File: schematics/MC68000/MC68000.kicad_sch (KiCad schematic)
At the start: 0 parts

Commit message: first commit
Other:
- note added: "CPU MC68000 CLOCK 16MHZ DATA AND ADDRESS BUFFERS HALT AND RESET DTACK GLUE LOGIC"
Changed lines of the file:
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@@
 (kicad_sch (version 20230121) (generator eeschema)
   (paper "A3")
-  (sheet (at 31.75 31.75) (size 60.96 16.51) (fields_autoplaced)
+  (text "CPU MC68000 \nCLOCK 16MHZ\nDATA AND ADDRESS BUFFERS\nHALT AND RESET\nDTACK GLUE LOGIC\n"
+    (at 36.83 57.15 0)
+    (effects (font (size 2.54 2.54) (thickness 0.254) bold) (justify left bottom))
+  )
+  (sheet (at 31.75 31.75) (size 80.01 30.48) (fields_autoplaced)
     (stroke (width 0.1524) (type solid))
     (fill (color 0 0 0 0.0000))
-    (property "Sheetname" "CPU" (at 31.75 31.0384 0)
-      (effects (font (size 1.27 1.27)) (justify left bottom))
+    (property "Sheetname" "CPU" (at 31.75 30.4034 0) (show_name)
+      (effects (font (size 2.54 2.54) bold) (justify left bottom))
     )
-    (property "Sheetfile" "cpu.kicad_sch" (at 31.75 48.8446 0)
-      (effects (font (size 1.27 1.27)) (justify left top))
+    (property "Sheetfile" "cpu.kicad_sch" (at 31.75 62.8146 0)
+      (effects (font (size 1.27 1.27)) (justify left top) hide)
     )
     (instances

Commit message: Update...
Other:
- added sheet MEMORY (memory.kicad_sch)
- note added: "CPU MC68000 CLOCK 16MHZ DATA AND ADDRESS BUFFERS HALT AND RESET DTACK GLUE LOGIC INTERRUPT"
- note added: "ROM 16kBytes RAM 1MBytes"
- note removed: "CPU MC68000 CLOCK 16MHZ DATA AND ADDRESS BUFFERS HALT AND RESET DTACK GLUE LOGIC"
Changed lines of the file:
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@@
 (kicad_sch (version 20230121) (generator eeschema)
   (paper "A3")
-  (text "CPU MC68000 \nCLOCK 16MHZ\nDATA AND ADDRESS BUFFERS\nHALT AND RESET\nDTACK GLUE LOGIC\n"
+  (text "ROM 16kBytes\nRAM 1MBytes\n" (at 34.29 83.82 0)
+    (effects (font (size 2.54 2.54) (thickness 0.508) bold) (justify left bottom))
+  )
+  (text "CPU MC68000 \nCLOCK 16MHZ\nDATA AND ADDRESS BUFFERS\nHALT AND RESET\nDTACK GLUE LOGIC\nINTERRUPT "
     (at 36.83 57.15 0)
     (effects (font (size 2.54 2.54) (thickness 0.254) bold) (justify left bottom))
   )
+  (sheet (at 31.75 72.39) (size 80.01 30.48) (fields_autoplaced)
+    (stroke (width 0.1524) (type solid))
+    (fill (color 0 0 0 0.0000))
+    (property "Sheetname" "MEMORY" (at 31.75 71.0434 0)
+      (effects (font (size 2.54 2.54)) (justify left bottom))
+    )
+    (property "Sheetfile" "memory.kicad_sch" (at 31.75 103.4546 0)
+      (effects (font (size 1.27 1.27)) (justify left top) hide)
+    )
+    (instances
+      (project "MC68000"
+        (path "/99c9748a-87b3-41bd-bdc2-3a5f137c7a40" (page "3"))
+      )
+    )
+  )
   (sheet (at 31.75 31.75) (size 80.01 30.48) (fields_autoplaced)

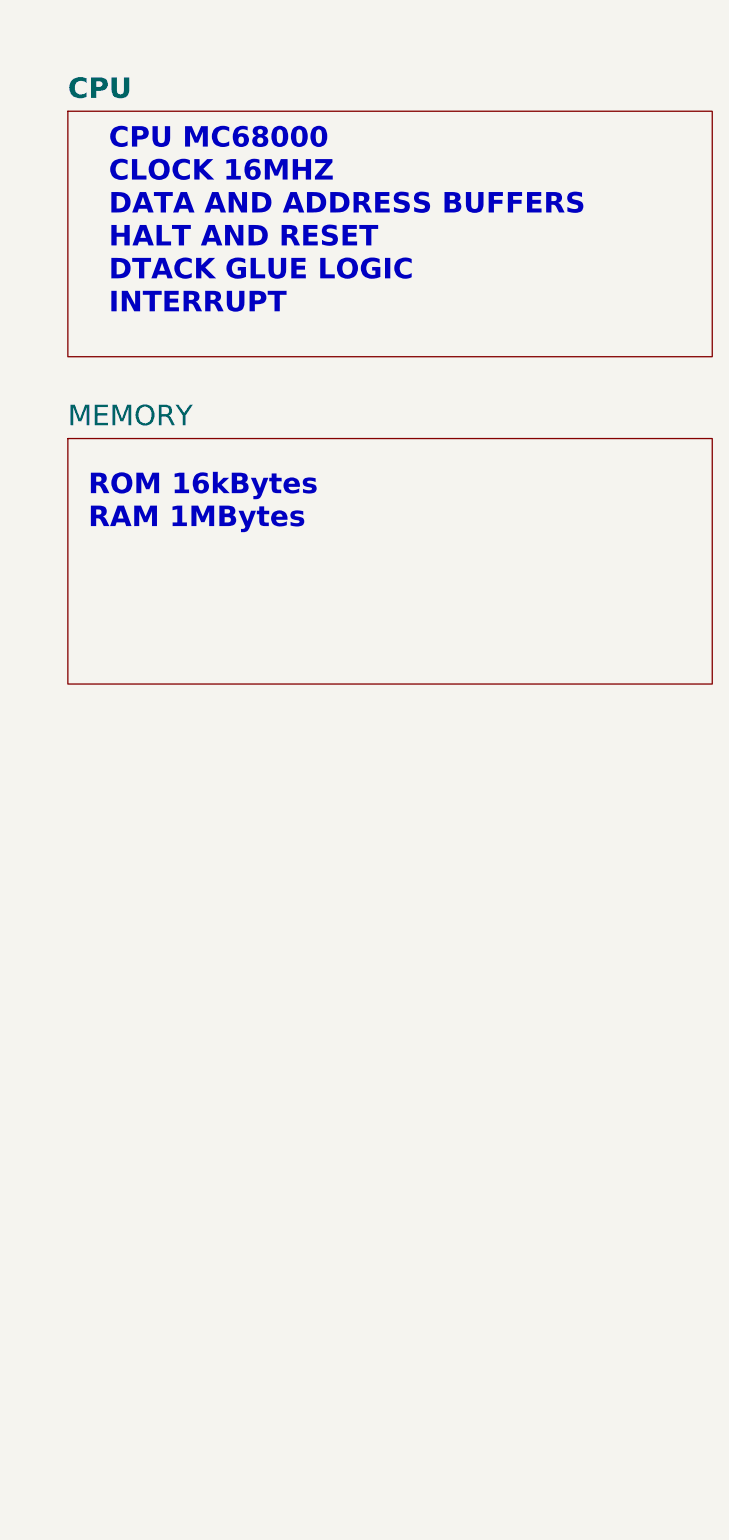
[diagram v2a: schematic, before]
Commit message: cleanup zips and added memory map equations for pld
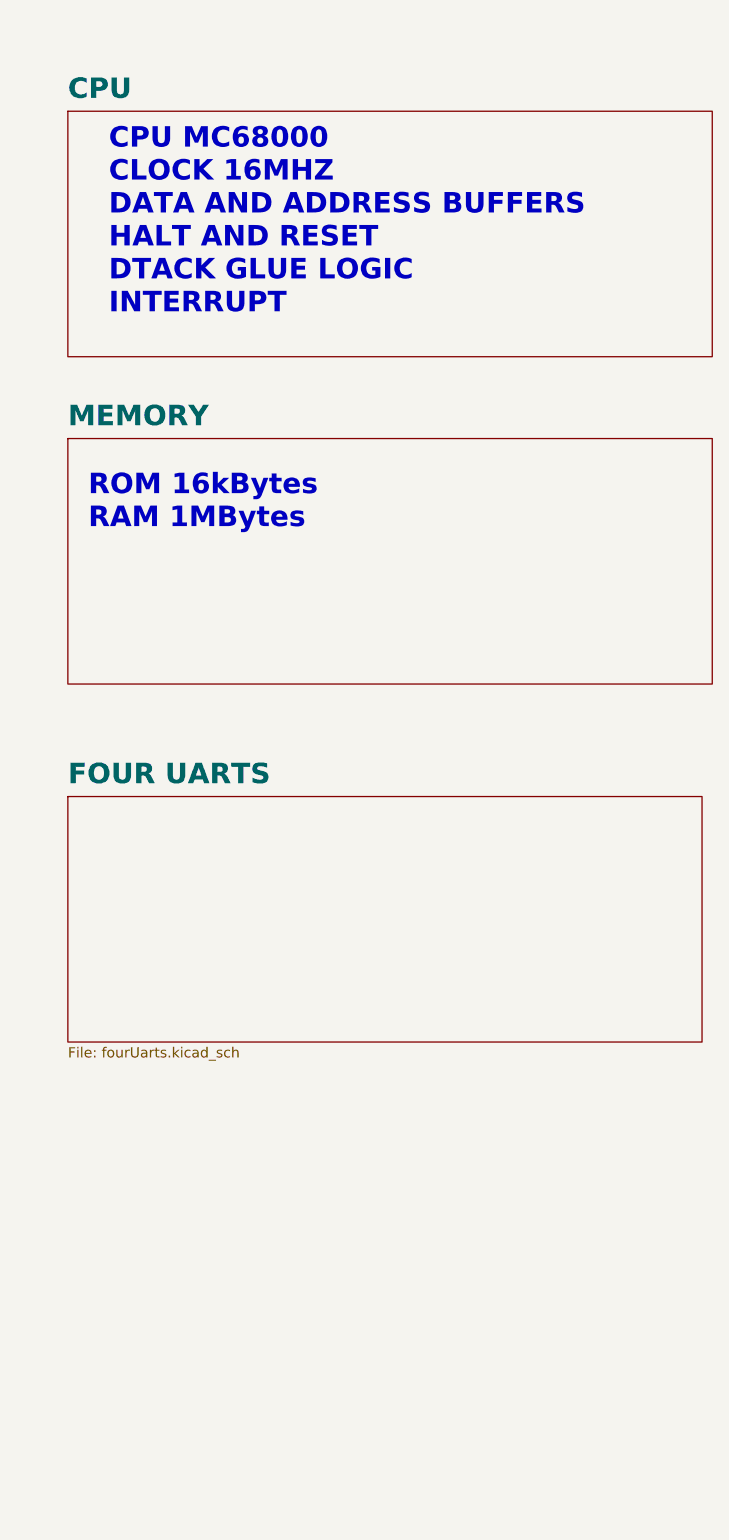
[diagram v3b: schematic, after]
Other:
- added sheet FOUR UARTS (fourUarts.kicad_sch)
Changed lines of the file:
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@@
     (fill (color 0 0 0 0.0000))
     (property "Sheetname" "MEMORY" (at 31.75 71.0434 0)
-      (effects (font (size 2.54 2.54)) (justify left bottom))
+      (effects (font (size 2.54 2.54) bold) (justify left bottom))
     )
     (property "Sheetfile" "memory.kicad_sch" (at 31.75 103.4546 0)
@@
       )
     )
+  )
+  (sheet (at 31.75 116.84) (size 78.74 30.48) (fields_autoplaced)
+    (stroke (width 0.1524) (type solid))
+    (fill (color 0 0 0 0.0000))
+    (property "Sheetname" "FOUR UARTS" (at 31.75 115.4934 0) (show_name)
+      (effects (font (size 2.54 2.54) bold) (justify left bottom))
+    )
+    (property "Sheetfile" "fourUarts.kicad_sch" (at 31.75 147.9046 0)
+      (effects (font (size 1.27 1.27)) (justify left top))
+    )
+    (instances
+      (project "MC68000"
+        (path "/99c9748a-87b3-41bd-bdc2-3a5f137c7a40" (page "4"))
+      )
+    )

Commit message: added schemati for cpu without buffers
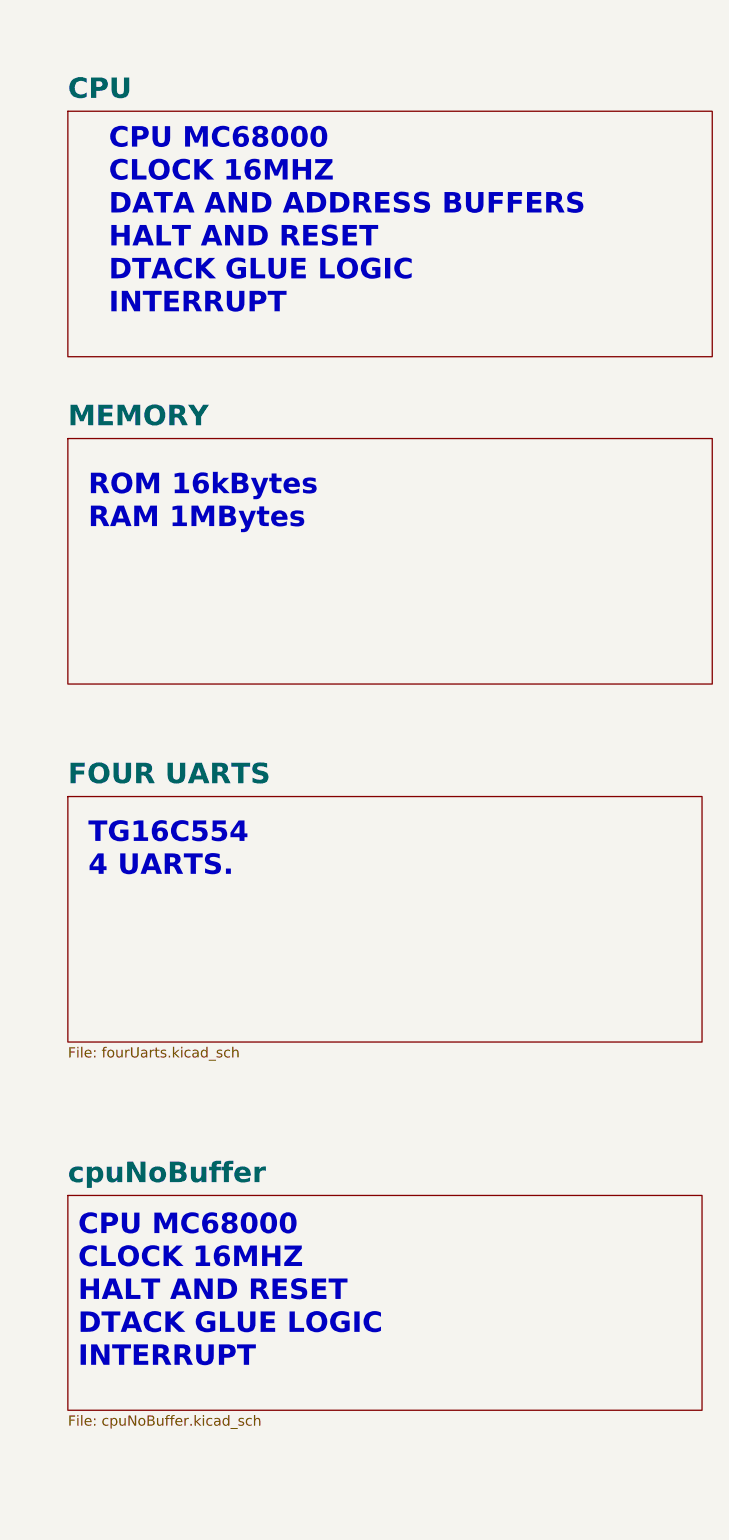
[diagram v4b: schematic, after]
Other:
- added sheet cpuNoBuffer (cpuNoBuffer.kicad_sch)
- note added: "CPU MC68000 CLOCK 16MHZ HALT AND RESET DTACK GLUE LOGIC INTERRUPT"
- note added: "TG16C554 4 UARTS."
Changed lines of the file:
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@@
     (effects (font (size 2.54 2.54) (thickness 0.254) bold) (justify left bottom))
+  )
+  (text "CPU MC68000 \nCLOCK 16MHZ\nHALT AND RESET\nDTACK GLUE LOGIC\nINTERRUPT "
+    (at 33.02 187.96 0)
+    (effects (font (size 2.54 2.54) (thickness 0.508) bold) (justify left bottom))
+  )
+  (text "TG16C554\n4 UARTS.\n" (at 34.29 127 0)
+    (effects (font (size 2.54 2.54) (thickness 0.508) bold) (justify left bottom))
   )
   (sheet (at 31.75 72.39) (size 80.01 30.48) (fields_autoplaced)
     (stroke (width 0.1524) (type solid))
     (fill (color 0 0 0 0.0000))
-    (property "Sheetname" "MEMORY" (at 31.75 71.0434 0)
+    (property "Sheetname" "MEMORY" (at 31.75 71.0434 0) (show_name)
       (effects (font (size 2.54 2.54) bold) (justify left bottom))
     )
@@
       )
     )
+  )
+  (sheet (at 31.75 166.37) (size 78.74 26.67) (fields_autoplaced)
+    (stroke (width 0.1524) (type solid))
+    (fill (color 0 0 0 0.0000))
+    (property "Sheetname" "cpuNoBuffer" (at 31.75 165.0234 0) (show_name)
+      (effects (font (size 2.54 2.54) bold) (justify left bottom))
+    )
+    (property "Sheetfile" "cpuNoBuffer.kicad_sch" (at 31.75 193.6246 0)
+      (effects (font (size 1.27 1.27)) (justify left top))
+    )
+    (instances
+      (project "MC68000"
+        (path "/99c9748a-87b3-41bd-bdc2-3a5f137c7a40" (page "5"))
+      )
+    )

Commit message: Ram memory test 2 OK
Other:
- added sheet UART CONTROL (uart_control.kicad_sch)
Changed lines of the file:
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@@
 (kicad_sch (version 20230121) (generator eeschema)
   (paper "A3")
-  (text "ROM 16kBytes\nRAM 1MBytes\n" (at 34.29 83.82 0)
+  (text "ROM 16kBytes\nRAM 1MBytes\n" (at 27.94 73.66 0)
     (effects (font (size 2.54 2.54) (thickness 0.508) bold) (justify left bottom))
   )
   (text "CPU MC68000 \nCLOCK 16MHZ\nDATA AND ADDRESS BUFFERS\nHALT AND RESET\nDTACK GLUE LOGIC\nINTERRUPT "
-    (at 36.83 57.15 0)
+    (at 27.94 52.07 0)
     (effects (font (size 2.54 2.54) (thickness 0.254) bold) (justify left bottom))
   )
   (text "CPU MC68000 \nCLOCK 16MHZ\nHALT AND RESET\nDTACK GLUE LOGIC\nINTERRUPT "
-    (at 33.02 187.96 0)
+    (at 27.94 161.29 0)
     (effects (font (size 2.54 2.54) (thickness 0.508) bold) (justify left bottom))
   )
-  (text "TG16C554\n4 UARTS.\n" (at 34.29 127 0)
+  (text "TG16C554\n4 UARTS.\n" (at 27.94 113.03 0)
     (effects (font (size 2.54 2.54) (thickness 0.508) bold) (justify left bottom))
   )
-  (sheet (at 31.75 72.39) (size 80.01 30.48) (fields_autoplaced)
+  (sheet (at 25.4 63.5) (size 80.01 30.48) (fields_autoplaced)
     (stroke (width 0.1524) (type solid))
     (fill (color 0 0 0 0.0000))
-    (property "Sheetname" "MEMORY" (at 31.75 71.0434 0) (show_name)
+    (property "Sheetname" "MEMORY" (at 25.4 62.1534 0) (show_name)
       (effects (font (size 2.54 2.54) bold) (justify left bottom))
     )
-    (property "Sheetfile" "memory.kicad_sch" (at 31.75 103.4546 0)
+    (property "Sheetfile" "memory.kicad_sch" (at 25.4 94.5646 0)
       (effects (font (size 1.27 1.27)) (justify left top) hide)
     )
@@
     )
   )
-  (sheet (at 31.75 116.84) (size 78.74 30.48) (fields_autoplaced)
+  (sheet (at 25.4 101.6) (size 80.01 26.67) (fields_autoplaced)
     (stroke (width 0.1524) (type solid))
     (fill (color 0 0 0 0.0000))
-    (property "Sheetname" "FOUR UARTS" (at 31.75 115.4934 0) (show_name)
+    (property "Sheetname" "FOUR UARTS" (at 25.4 100.2534 0) (show_name)
       (effects (font (size 2.54 2.54) bold) (justify left bottom))
     )
-    (property "Sheetfile" "fourUarts.kicad_sch" (at 31.75 147.9046 0)
+    (property "Sheetfile" "fourUarts.kicad_sch" (at 25.4 128.8546 0)
       (effects (font (size 1.27 1.27)) (justify left top))
     )
@@
     )
   )
-  (sheet (at 31.75 31.75) (size 80.01 30.48) (fields_autoplaced)
+  (sheet (at 25.4 25.4) (size 80.01 30.48) (fields_autoplaced)
     (stroke (width 0.1524) (type solid))
     (fill (color 0 0 0 0.0000))
-    (property "Sheetname" "CPU" (at 31.75 30.4034 0) (show_name)
+    (property "Sheetname" "CPU" (at 25.4 24.0534 0) (show_name)
       (effects (font (size 2.54 2.54) bold) (justify left bottom))
     )
-    (property "Sheetfile" "cpu.kicad_sch" (at 31.75 62.8146 0)
+    (property "Sheetfile" "cpu.kicad_sch" (at 25.4 56.4646 0)
       (effects (font (size 1.27 1.27)) (justify left top) hide)
     )
@@
     )
   )
-  (sheet (at 31.75 166.37) (size 78.74 26.67) (fields_autoplaced)
+  (sheet (at 25.4 179.07) (size 77.47 25.4) (fields_autoplaced)
     (stroke (width 0.1524) (type solid))
     (fill (color 0 0 0 0.0000))
-    (property "Sheetname" "cpuNoBuffer" (at 31.75 165.0234 0) (show_name)
+    (property "Sheetname" "UART CONTROL" (at 25.4 178.3584 0)
+      (effects (font (size 1.27 1.27)) (justify left bottom))
+    )
+    (property "Sheetfile" "uart_control.kicad_sch" (at 25.4 205.0546 0)
+      (effects (font (size 1.27 1.27)) (justify left top))
+    )
+    (instances
+      (project "MC68000"
+        (path "/99c9748a-87b3-41bd-bdc2-3a5f137c7a40" (page "6"))
+      )
+    )
+  )
+  (sheet (at 25.4 139.7) (size 80.01 26.67) (fields_autoplaced)
+    (stroke (width 0.1524) (type solid))
+    (fill (color 0 0 0 0.0000))
+    (property "Sheetname" "cpuNoBuffer" (at 25.4 138.3534 0) (show_name)
       (effects (font (size 2.54 2.54) bold) (justify left bottom))
     )
-    (property "Sheetfile" "cpuNoBuffer.kicad_sch" (at 31.75 193.6246 0)
+    (property "Sheetfile" "cpuNoBuffer.kicad_sch" (at 25.4 166.9546 0)
       (effects (font (size 1.27 1.27)) (justify left top))
     )
